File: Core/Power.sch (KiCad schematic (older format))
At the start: 42 parts, among them J21 Conn_02x08_Odd_Even, U10 TL072, U11 TL072, U12 TL072, U13 TL072, U18 MIC5504-3.3YM5

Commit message: Add custom footprints and symbols
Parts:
- J21: footprint CustomLib:Header_2x8_Shrouded_SMD -> Custom_FP:Header_2x8_Shrouded_SMD
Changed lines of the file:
@@
 F 0 "J21" H 1700 7517 50  0000 C CNN
 F 1 "Conn_02x08_Odd_Even" H 1700 7426 50  0000 C CNN
-F 2 "CustomLib:Header_2x8_Shrouded_SMD" H 1650 7000 50  0001 C CNN
+F 2 "Custom_FP:Header_2x8_Shrouded_SMD" H 1650 7000 50  0001 C CNN
 F 3 "~" H 1650 7000 50  0001 C CNN
 	1    1650 7000

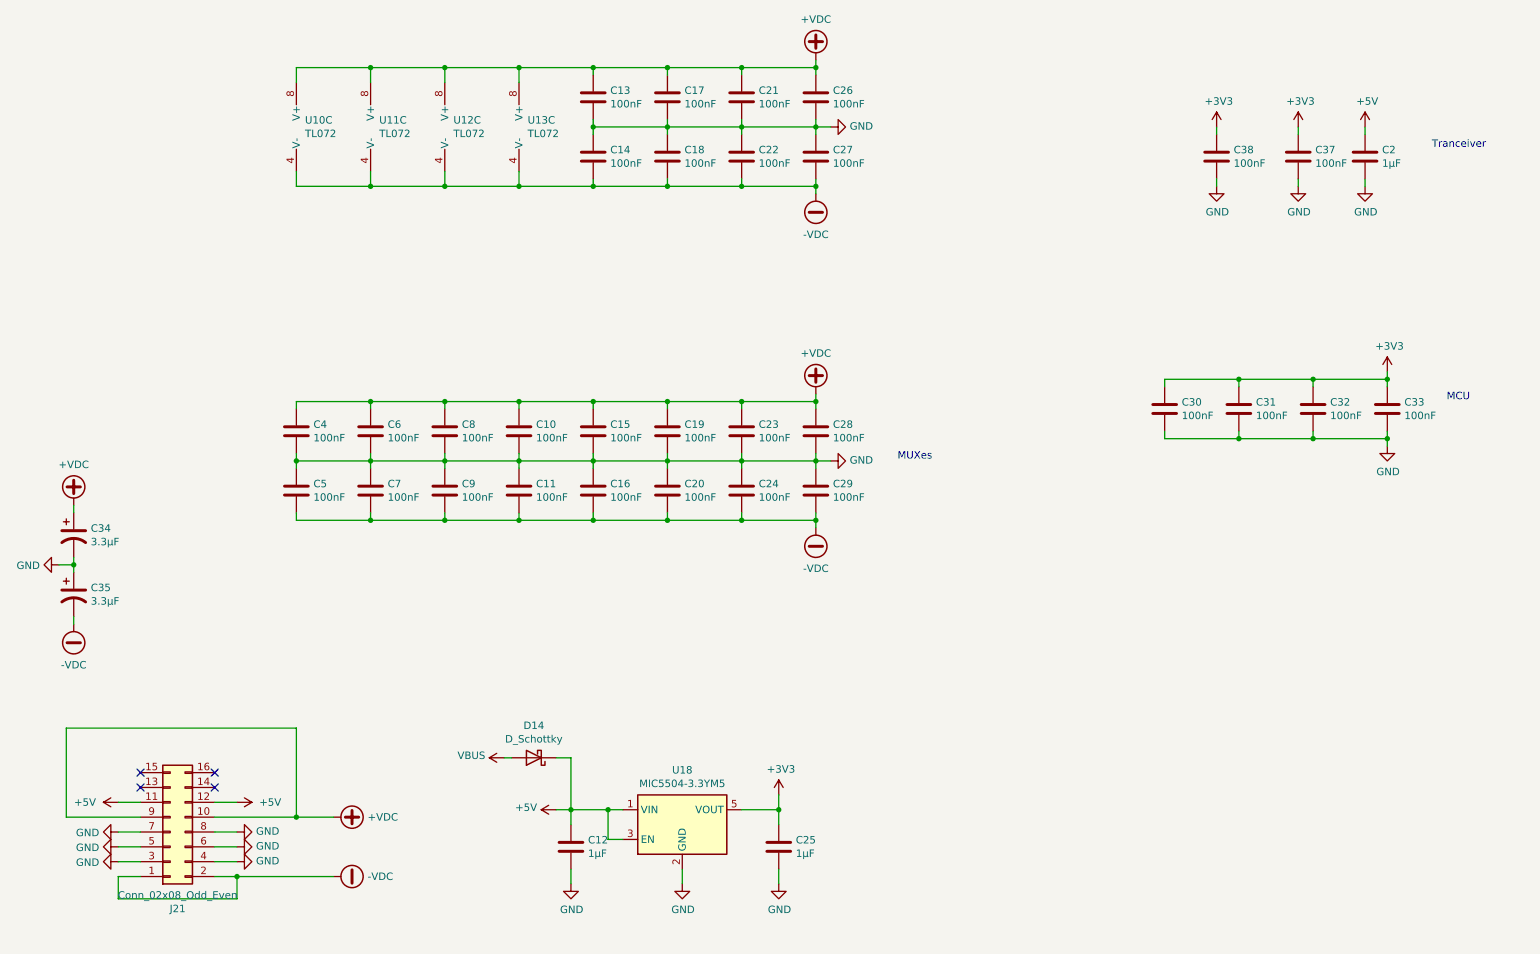
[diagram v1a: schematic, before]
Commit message: Add shift-registers+++
Added shift-registers
Added power protection
Changed USB footprint
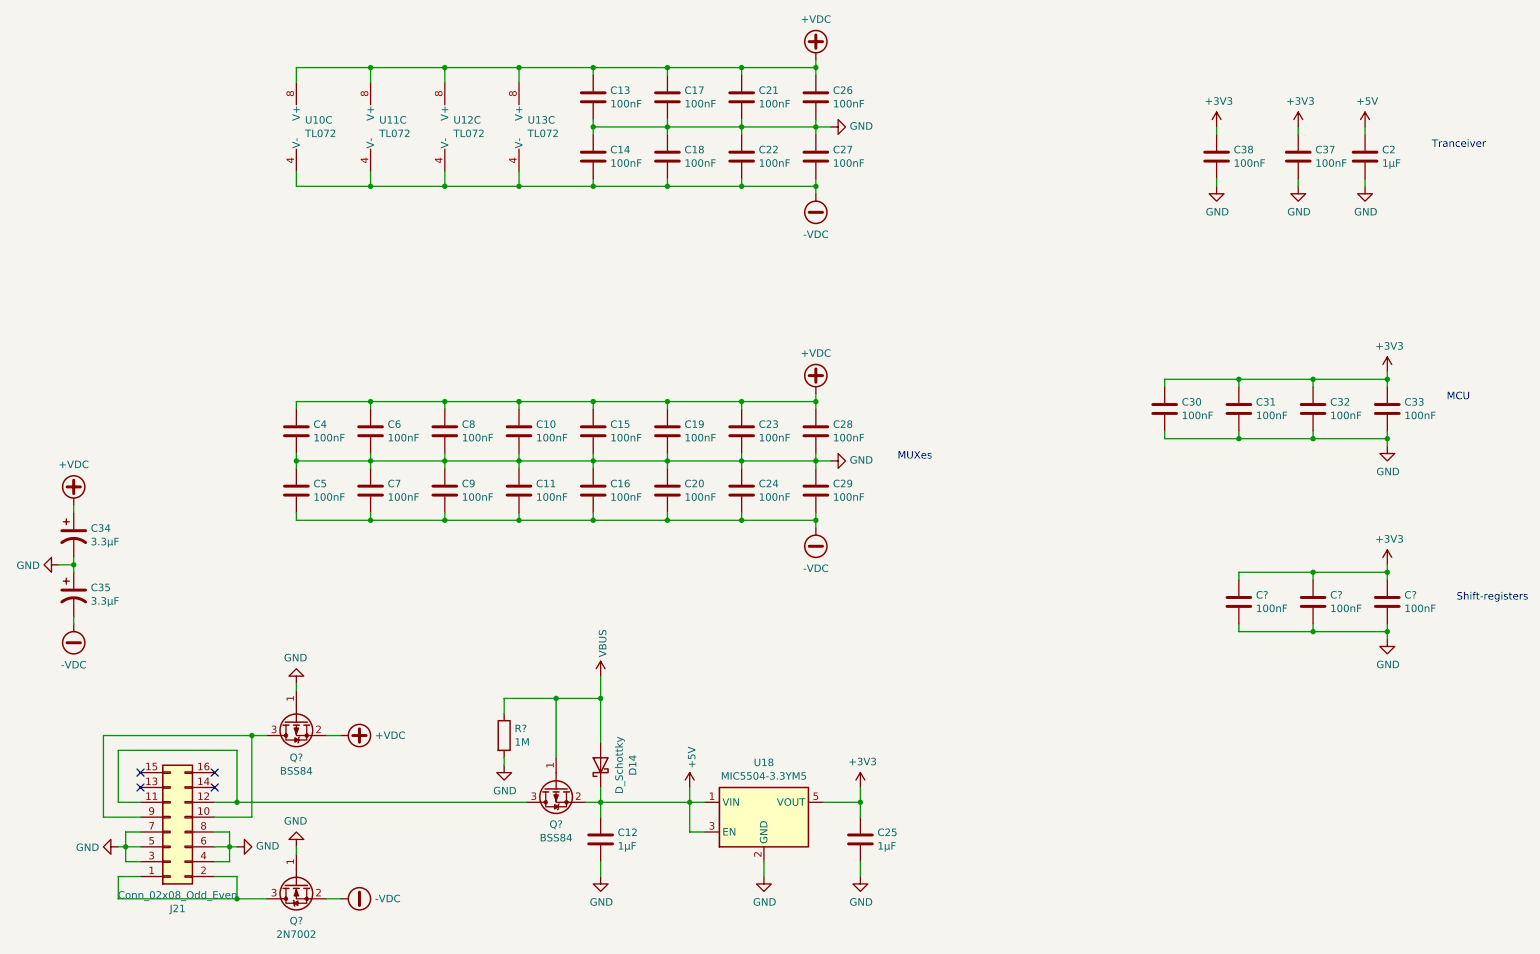
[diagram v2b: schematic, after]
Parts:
- added C? (x3): 100nF, Capacitor_SMD:C_0603_1608Metric, symbol Device:C
- added Q? (x2): BSS84, Package_TO_SOT_SMD:SOT-23, symbol Transistor_FET:BSS84
- added Q?: 2N7002, Package_TO_SOT_SMD:SOT-23, symbol Transistor_FET:2N7002
- added R?: 1M, symbol Device:R
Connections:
- net +3V3: now also C?.1, C?.1, C?.1
- net +5V: now also Q?.2 (S); no longer J21.11 (Pin_11), J21.12 (Pin_12)
- net +VDC: now also Q?.2 (S); no longer J21.10 (Pin_10), J21.9 (Pin_9)
- net -VDC: now also Q?.2 (S); no longer J21.1 (Pin_1), J21.2 (Pin_2)
- net GND: now also C?.2, C?.2, C?.2, Q?.1 (G), Q?.1 (G), R?.2
- net VBUS: now also Q?.1 (G), R?.1
- new net: J21.1 (Pin_1), J21.2 (Pin_2), Q?.3 (D)
- new net: J21.10 (Pin_10), J21.9 (Pin_9), Q?.3 (D)
- new net: J21.11 (Pin_11), J21.12 (Pin_12), Q?.3 (D)
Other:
- note added: "Shift-registers"
- moved on the sheet: C12, C25, D14, U18

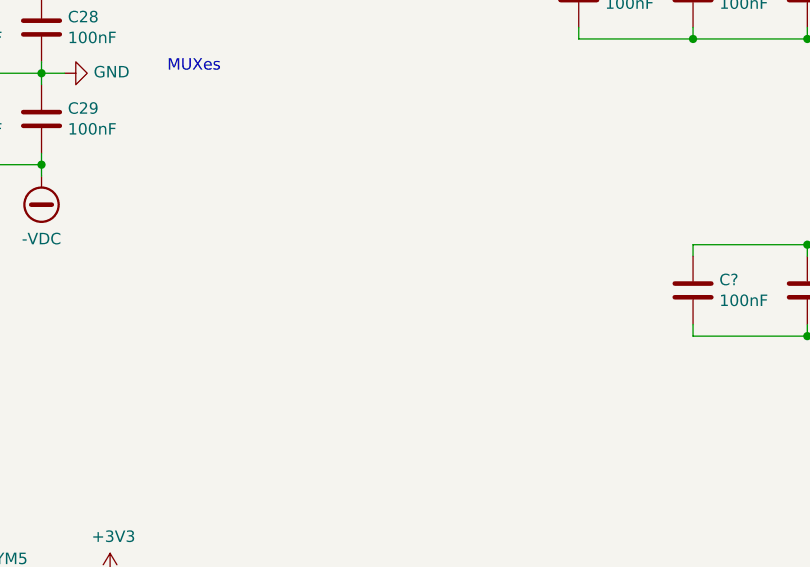
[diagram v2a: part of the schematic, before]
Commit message: Add EEPROM
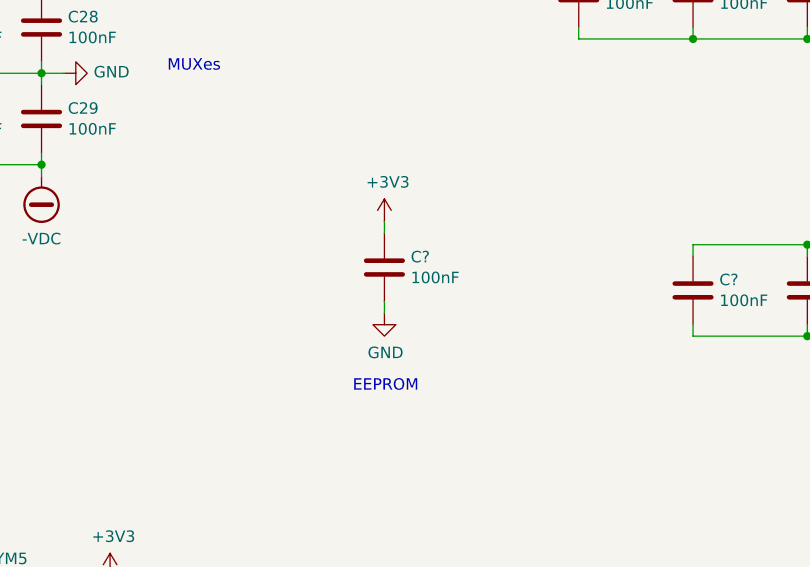
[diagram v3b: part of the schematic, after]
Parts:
- added C?: 100nF, Capacitor_SMD:C_0603_1608Metric, symbol Device:C
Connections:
- net +3V3: now also C?.1
- net GND: now also C?.2
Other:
- note added: "EEPROM"
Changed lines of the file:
@@
 Wire Wire Line
 	3900 6500 3900 6550
+Text Notes 7650 5900 2    50   ~ 0
+EEPROM
+$Comp
+L Device:C C?
+U 1 1 651C0563
+P 7500 5350
+F 0 "C?" H 7615 5396 50  0000 L CNN
+F 1 "100nF" H 7615 5305 50  0000 L CNN
+F 2 "Capacitor_SMD:C_0603_1608Metric" H 7538 5200 50  0001 C CNN
+F 3 "~" H 7500 5350 50  0001 C CNN
+	1    7500 5350
+	1    0    0    -1
+$EndComp
+Wire Wire Line
+	7500 5550 7500 5500
+Wire Wire Line
+	7500 5200 7500 5150
+$Comp
+L power:+3V3 #PWR?
+U 1 1 651C0E37
+P 7500 5150
+F 0 "#PWR?" H 7500 5000 50  0001 C CNN
+F 1 "+3V3" H 7515 5323 50  0000 C CNN
+F 2 "" H 7500 5150 50  0001 C CNN
+F 3 "" H 7500 5150 50  0001 C CNN
+	1    7500 5150
+	1    0    0    -1
+$EndComp
+$Comp
+L power:GND #PWR?
+U 1 1 651C0E41
+P 7500 5550
+F 0 "#PWR?" H 7500 5300 50  0001 C CNN
+F 1 "GND" H 7505 5377 50  0000 C CNN
+F 2 "" H 7500 5550 50  0001 C CNN
+F 3 "" H 7500 5550 50  0001 C CNN
+	1    7500 5550
+	1    0    0    -1
+$EndComp
 $EndSCHEMATC
